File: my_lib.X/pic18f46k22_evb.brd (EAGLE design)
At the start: 100 x 80 mm, 82 parts, among them IC2 PCF8583P, J1 POWER_JACKSLT, U1 PIC18F46K22, U2 LCD-16X2NOHOLES

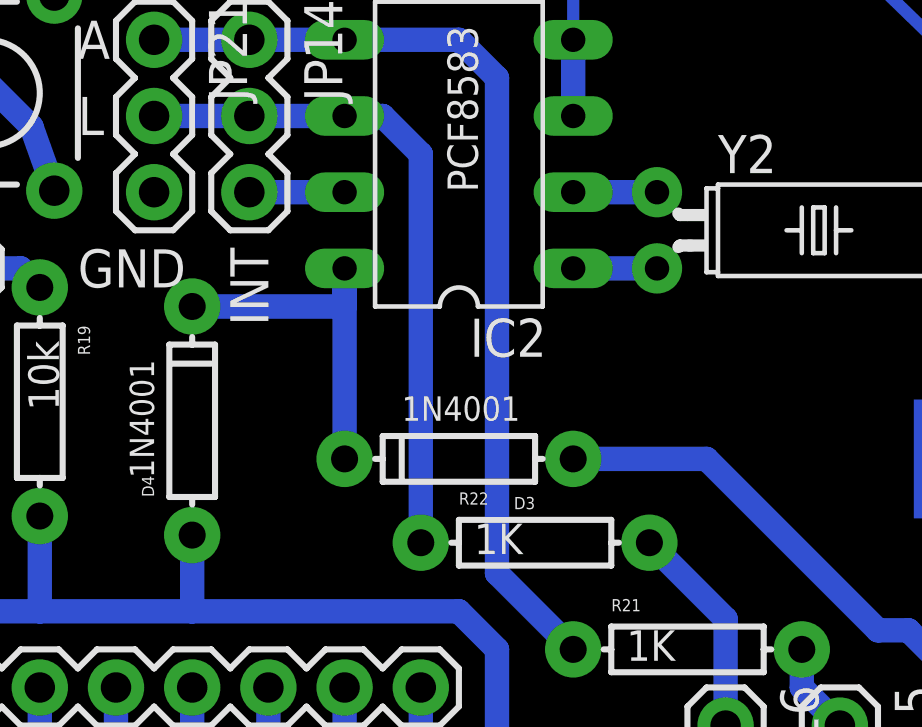
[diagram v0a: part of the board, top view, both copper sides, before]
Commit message: Corrections at schematic and pcb of the evaluation board based on PIC18F46K22
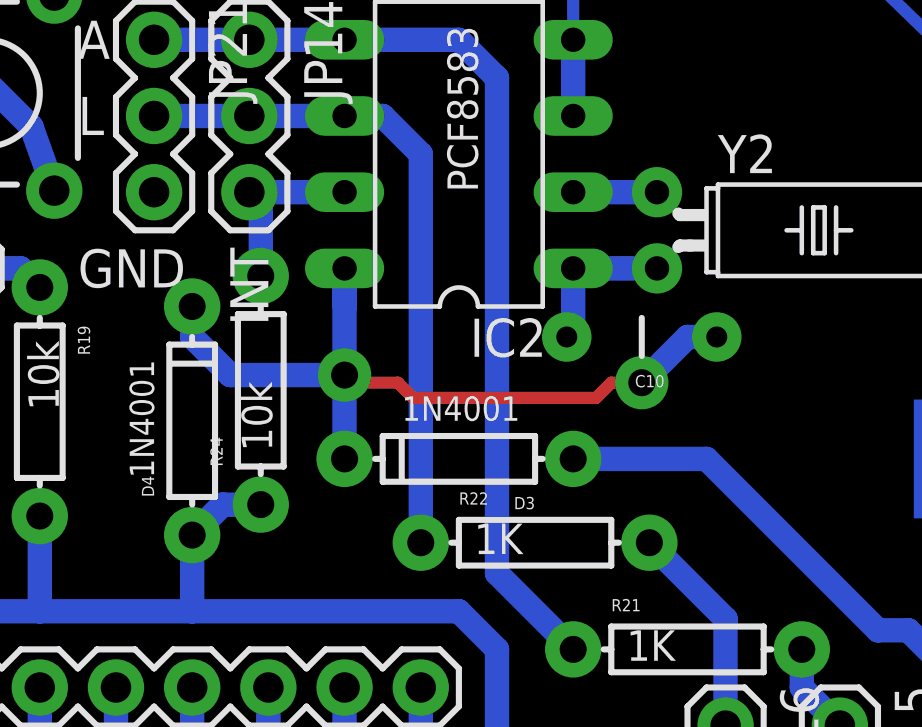
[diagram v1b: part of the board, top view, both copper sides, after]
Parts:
- added C10: 22pF, SparkFun-Passives:CAP-PTH-5MM
- added R24: 10k, SparkFun-Resistors:AXIAL-0.3
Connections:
- net 5VCC: now also R24.P$1
- net N$14: now also C10.2
- net N$29: now also C10.1
- net N$30: now also R24.P$2
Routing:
- net N$29: track 12.7 -> 27.8 mm, vias 0 -> 2
- net N$30: track 3.17 -> 6.13 mm
- net 5VCC: track 363.1 -> 365.8 mm
- net N$14: track 2.79 -> 5.29 mm
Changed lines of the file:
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@@
 <element name="DZ2" library="SparkFun-DiscreteSemi" package="DIODE-ZENER" value="5V1" x="44.45" y="15.24"/>
 <element name="JP21" library="SparkFun-Connectors" package="1X03" value="" x="67.31" y="74.93" rot="R270"/>
+<element name="C10" library="SparkFun-Passives" package="CAP-PTH-5MM" value="22pF" x="83.566" y="65.024" rot="R180"/>
+<element name="R24" library="SparkFun-Resistors" package="AXIAL-0.3" value="10k" x="70.866" y="63.246" rot="R90"/>
 </elements>
 <signals>
@@
 <wire x1="80.01" y1="41.91" x2="87.63" y2="41.91" width="0.8128" layer="16"/>
 <wire x1="86.36" y1="49.53" x2="78.74" y2="49.53" width="0.8128" layer="16"/>
+<contactref element="R24" pad="P$1"/>
+<wire x1="70.866" y1="59.436" x2="69.596" y2="59.436" width="0.8128" layer="16"/>
+<wire x1="69.596" y1="59.436" x2="68.58" y2="58.42" width="0.8128" layer="16"/>
 <wire x1="92.71" y1="25.4" x2="93.23605" y2="25.29105" width="0" layer="19" extent="16-16"/>
 </signal>
@@
 <contactref element="Y2" pad="2"/>
 <wire x1="84.074" y1="67.31" x2="81.28" y2="67.31" width="0.8128" layer="16"/>
+<contactref element="C10" pad="2"/>
+<wire x1="81.066" y1="65.024" x2="81.28" y2="65.024" width="0.8128" layer="16"/>
+<wire x1="81.28" y1="65.024" x2="81.28" y2="67.31" width="0.8128" layer="16"/>
 </signal>
 <signal name="D4">
@@
 <contactref element="JP14" pad="3"/>
 <wire x1="70.485" y1="69.85" x2="73.66" y2="69.85" width="0.8128" layer="16"/>
+<contactref element="R24" pad="P$2"/>
+<wire x1="70.866" y1="67.056" x2="70.866" y2="69.469" width="0.8128" layer="16"/>
+<wire x1="70.866" y1="69.469" x2="70.485" y2="69.85" width="0.8128" layer="16"/>
 </signal>
 <signal name="SCL">
@@
 <contactref element="D4" pad="C"/>
 <contactref element="D3" pad="C"/>
-<wire x1="68.58" y1="66.04" x2="73.66" y2="66.04" width="0.8128" layer="16"/>
 <wire x1="73.66" y1="66.04" x2="73.66" y2="67.31" width="0.8128" layer="16"/>
-<wire x1="73.66" y1="67.31" x2="73.66" y2="60.96" width="0.8128" layer="16"/>
+<wire x1="73.66" y1="67.31" x2="73.66" y2="63.754" width="0.8128" layer="16"/>
+<contactref element="C10" pad="1"/>
+<wire x1="73.66" y1="63.754" x2="73.66" y2="60.96" width="0.8128" layer="16"/>
+<wire x1="86.066" y1="65.024" x2="85.09" y2="65.024" width="0.8128" layer="16"/>
+<wire x1="85.09" y1="65.024" x2="83.566" y2="63.5" width="0.8128" layer="16"/>
+<via x="83.566" y="63.5" extent="1-16" drill="0.9" diameter="1.778"/>
+<wire x1="83.566" y1="63.5" x2="82.55" y2="63.5" width="0.4064" layer="1"/>
+<wire x1="82.55" y1="63.5" x2="82.042" y2="62.992" width="0.4064" layer="1"/>
+<wire x1="82.042" y1="62.992" x2="75.946" y2="62.992" width="0.4064" layer="1"/>
+<wire x1="75.946" y1="62.992" x2="75.438" y2="63.5" width="0.4064" layer="1"/>
+<wire x1="75.438" y1="63.5" x2="73.914" y2="63.5" width="0.4064" layer="1"/>
+<wire x1="73.914" y1="63.5" x2="73.66" y2="63.754" width="0.8128" layer="1"/>
+<via x="73.66" y="63.754" extent="1-16" drill="0.9" diameter="1.778"/>
+<wire x1="68.58" y1="66.04" x2="68.58" y2="65.024" width="0.8128" layer="16"/>
+<wire x1="68.58" y1="65.024" x2="69.85" y2="63.754" width="0.8128" layer="16"/>
+<wire x1="69.85" y1="63.754" x2="73.66" y2="63.754" width="0.8128" layer="16"/>
 </signal>
 </signals>
